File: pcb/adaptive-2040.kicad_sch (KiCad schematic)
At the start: 20 parts, among them J1 USB_A, J10 AudioJack2, J11 AudioJack2, J12 AudioJack2, J13 AudioJack2, J14 AudioJack2, J15 AudioJack2, J16 AudioJack2, J17 AudioJack2, J18 AudioJack2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

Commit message: tidy things up a little
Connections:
- no-connect marks 0 -> 12
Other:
- company: (none) -> moth.monster
- title: (none) -> adaptive2040
- moved on the sheet: J1, J10, J11, J12, J13, J14, J15, J16, J17, J18, J19, J2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

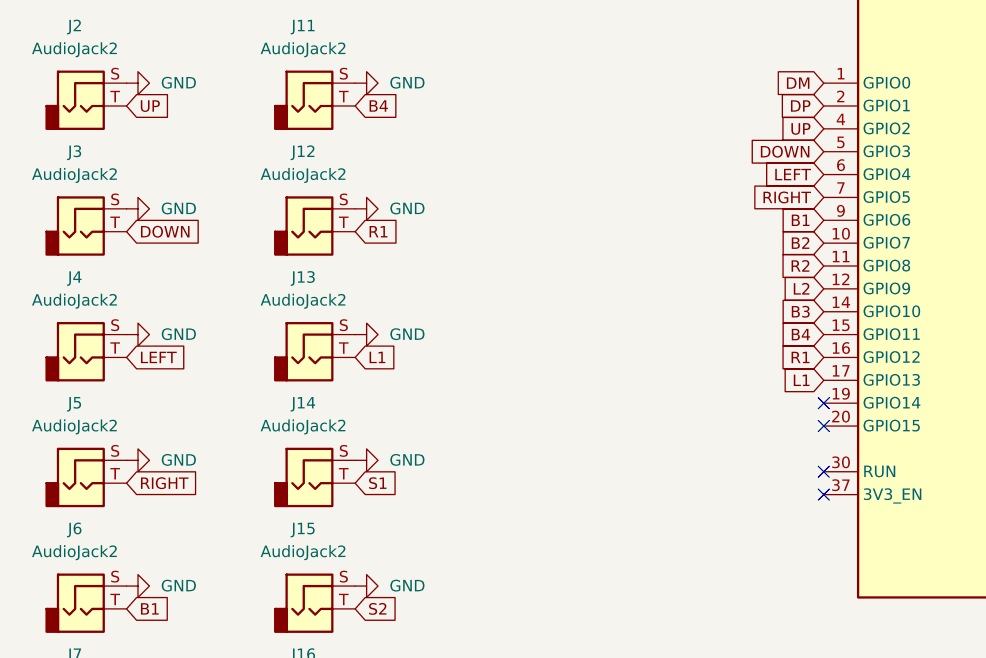
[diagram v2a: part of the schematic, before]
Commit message: r1.1 - fix silkscreen error
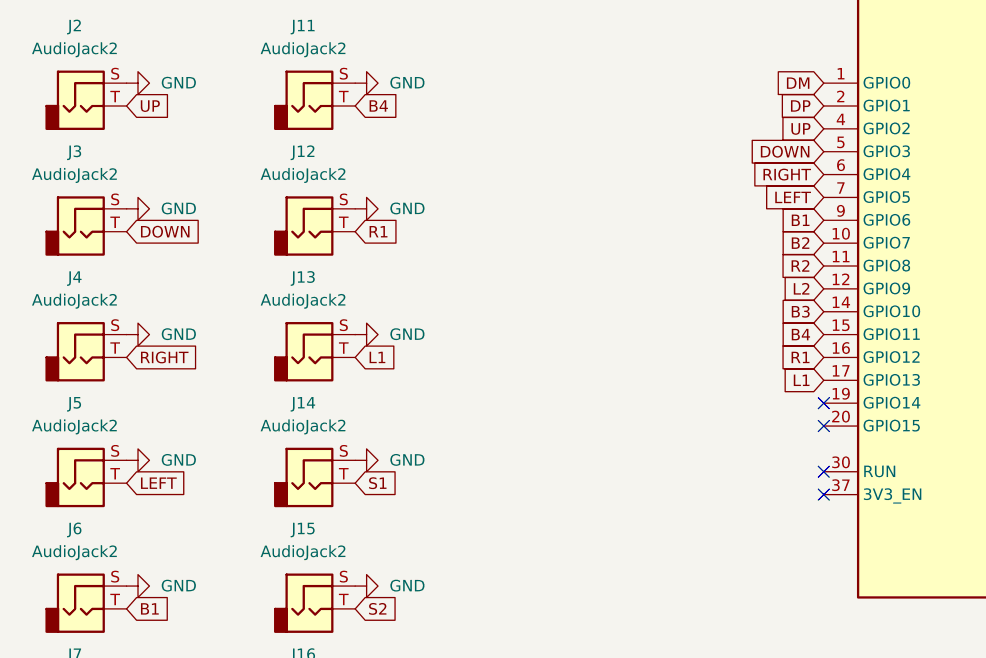
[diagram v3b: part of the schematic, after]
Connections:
- net LEFT: now also J5.T, U1.7 (GPIO5); no longer J4.T, U1.6 (GPIO4)
- net RIGHT: now also J4.T, U1.6 (GPIO4); no longer J5.T, U1.7 (GPIO5)
